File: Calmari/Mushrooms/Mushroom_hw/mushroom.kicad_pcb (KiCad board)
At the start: 2 copper layers, 114 x 16 mm, 56 parts, among them M1 MOTOR_PAD, Q1 MMBT2222, Q2 MMBT2222, Q3 LED_RGB 5050

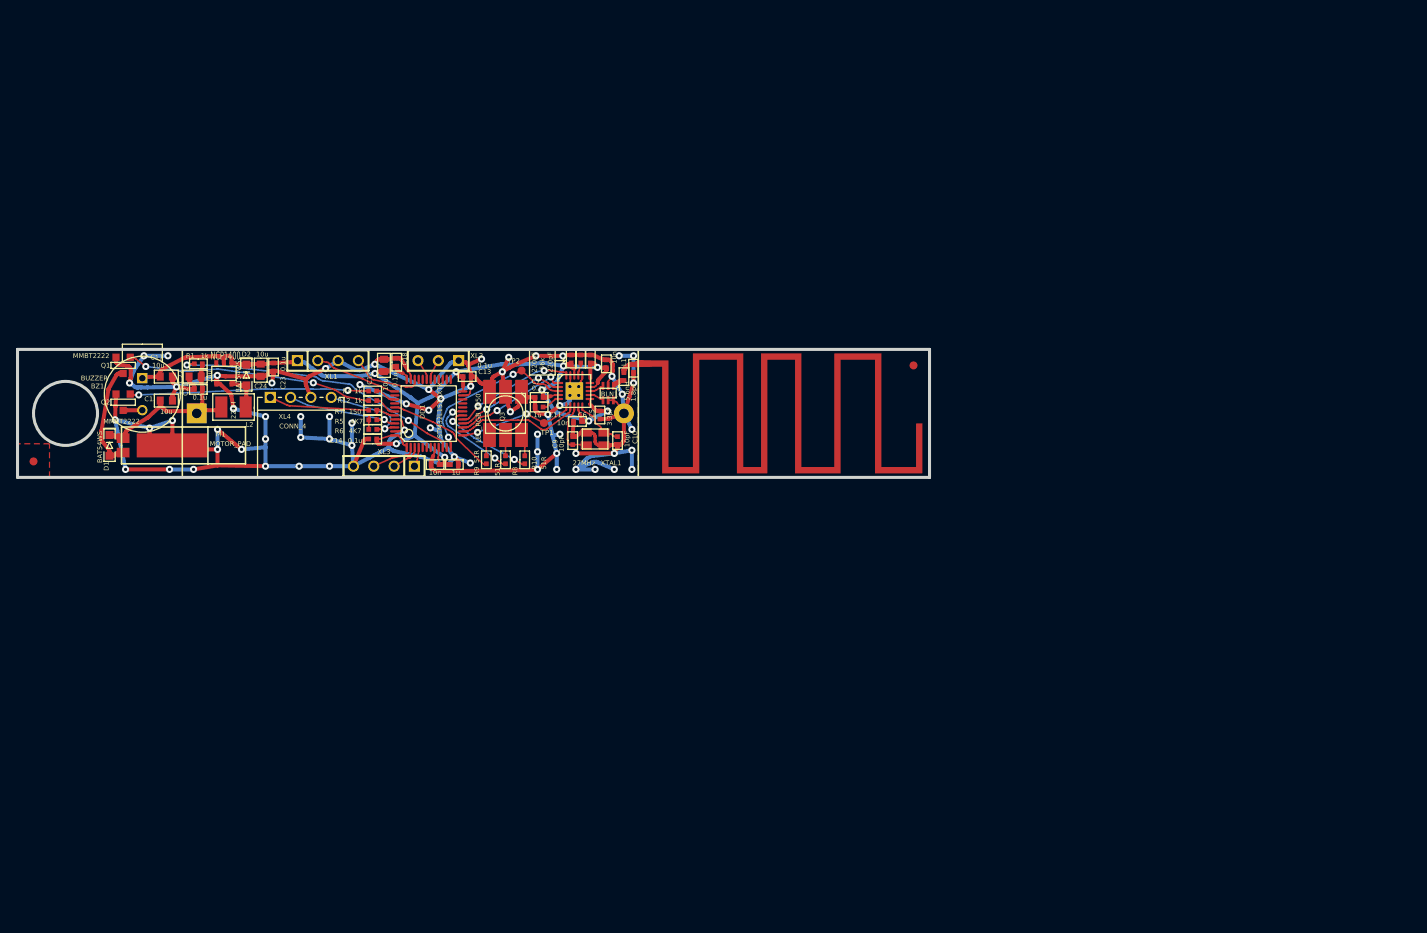
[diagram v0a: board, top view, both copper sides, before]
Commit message: 
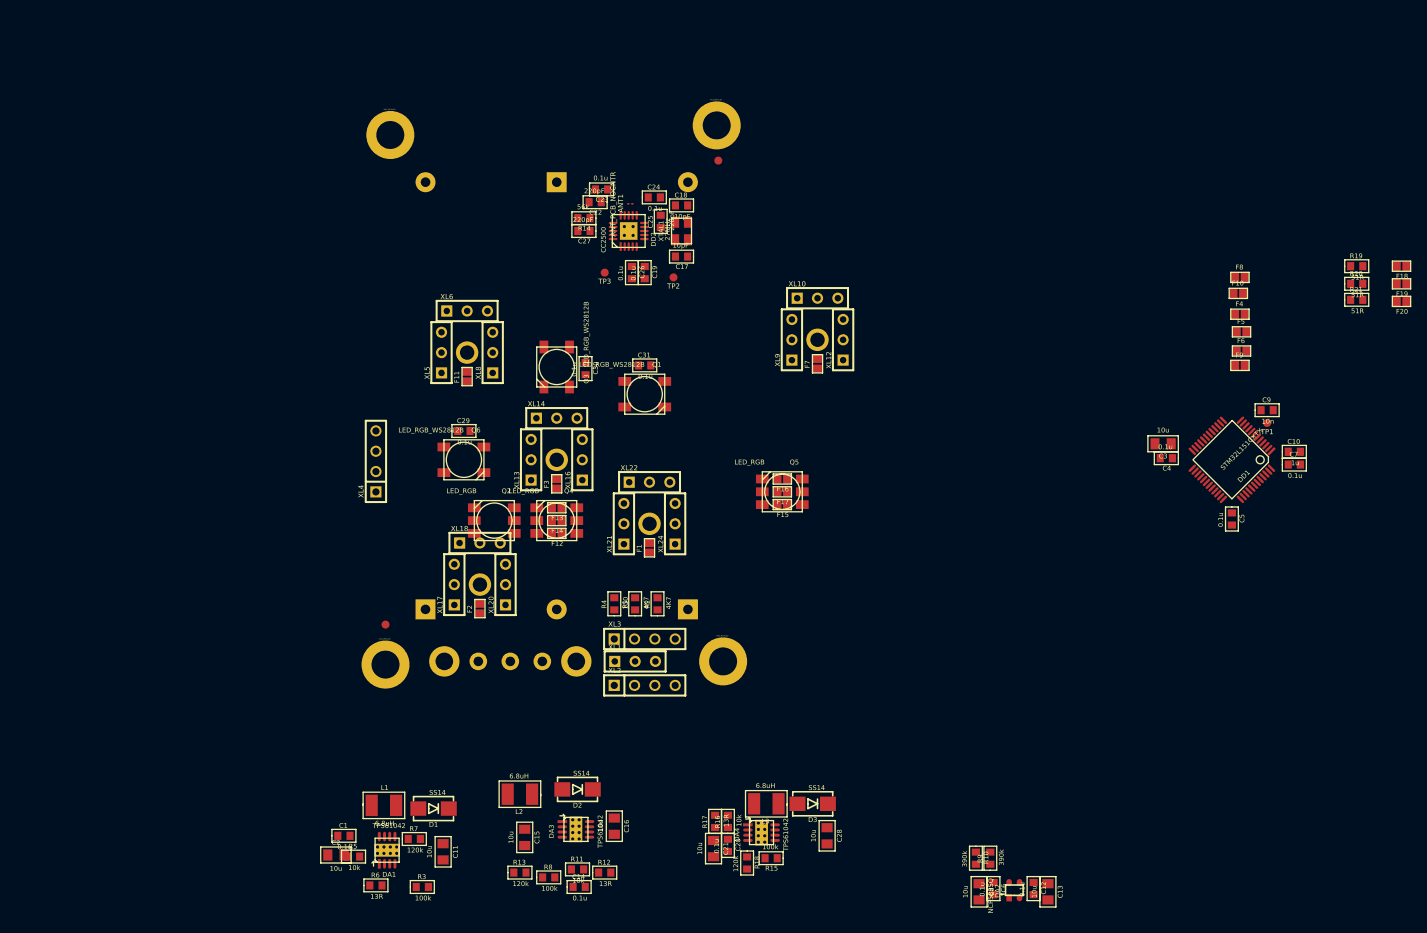
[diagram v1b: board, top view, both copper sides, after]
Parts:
- removed BLN1: 0896BM15A0001, BALUN_JOHANSON868
- removed BZ1: BUZZER, BUZZER_HC0903
- removed M1: MOTOR_PAD, MOTOR_KHN4NX
- added B1: BAT, BAT_AA, B.Cu at (243.8, 178.8)
- added B2: BAT, BAT_AA, B.Cu at (227.4, 178.8)
- added C19: 0.1u, CAP_0603, F.Cu at (238.4, 163.4)
- added C20: 0.1u, CAP_0603, F.Cu at (248.8, 235.0)
- added C25: 220pF, CAP_0603, F.Cu at (240.4, 157.0)
- added C26: 0.1u, CAP_0603, F.Cu at (236.8, 163.4)
- added C27: 220pF, CAP_0603, F.Cu at (230.8, 158.2)
- added C28: 10u, CAP_0805, F.Cu at (261.2, 233.8)
- added C29: 0.1u, CAP_0603, F.Cu at (215.8, 183.2)
- added C30: 0.1u, CAP_0603, F.Cu at (231.0, 175.4)
- added C31: 0.1u, CAP_0603, F.Cu at (238.4, 175.0)
- added D3: SS14, DIODE_SMA_DO214AC, F.Cu at (259.4, 229.8)
- added DA2: NCP583SQ, SC82AB, F.Cu at (284.6, 240.6)
- added DA3: TPS61042, DRB8, F.Cu at (229.8, 233.0)
- added DA4: TPS61042, DRB8, F.Cu at (253.0, 233.4)
- added F1: FUSE0R, SMD0603_FUSE, F.Cu at (239.0, 197.8)
- added F10: FUSE0R, SMD0603_FUSE, F.Cu at (312.6, 166.0)
- added F11: FUSE0R, SMD0603_FUSE, F.Cu at (216.2, 176.4)
- added F12: FUSE0R, SMD0603_FUSE, F.Cu at (227.4, 196.0)
- added F13: FUSE0R, SMD0603_FUSE, F.Cu at (227.4, 192.8)
- added F14: FUSE0R, SMD0603_FUSE, F.Cu at (227.4, 194.4)
- added F15: FUSE0R, SMD0603_FUSE, F.Cu at (255.6, 192.4)
- added F16: FUSE0R, SMD0603_FUSE, F.Cu at (255.6, 189.2)
- added F17: FUSE0R, SMD0603_FUSE, F.Cu at (255.6, 190.8)
- added F18: FUSE0R, SMD0603_FUSE, F.Cu at (333.0, 162.6)
- added F19: FUSE0R, SMD0603_FUSE, F.Cu at (333.0, 164.8)
- added F2: FUSE0R, SMD0603_FUSE, F.Cu at (217.8, 205.4)
- added F20: FUSE0R, SMD0603_FUSE, F.Cu at (333.0, 167.0)
- added F3: FUSE0R, SMD0603_FUSE, F.Cu at (227.4, 189.8)
- added F4: FUSE0R, SMD0603_FUSE, F.Cu at (312.8, 168.6)
- added F5: FUSE0R, SMD0603_FUSE, F.Cu at (313.0, 170.8)
- added F6: FUSE0R, SMD0603_FUSE, F.Cu at (313.0, 173.2)
- added F7: FUSE0R, SMD0603_FUSE, F.Cu at (260.0, 174.8)
- added F8: FUSE0R, SMD0603_FUSE, F.Cu at (312.8, 164.0)
- added F9: FUSE0R, SMD0603_FUSE, F.Cu at (312.8, 175.0)
- added HOLE1: HOLE_METALLED, Hole3_5_out6mm, F.Cu at (206.6, 146.2)
- added HOLE2: HOLE_METALLED, Hole3_5_out6mm, F.Cu at (248.2, 212.0)
- added HOLE3: HOLE_METALLED, Hole3_5_out6mm, F.Cu at (206.0, 212.4)
- added HOLE4: HOLE_METALLED, Hole3_5_out6mm, F.Cu at (247.4, 145.0)
- added L3: 6.8uH, IND_1210, F.Cu at (253.6, 229.8)
- added Q4: LED_RGB, LED_HH5050_RGB, F.Cu at (227.4, 194.4)
- added Q5: LED_RGB, LED_HH5050_RGB, F.Cu at (255.6, 190.8)
- added Q6: LED_RGB_WS2812B, LED_WS2812B, F.Cu at (215.8, 186.8)
- added R11: 10k, RES_0603, F.Cu at (230.0, 238.0)
- added R13: 120k, RES_0603, F.Cu at (222.8, 238.4)
- added R14: 56k, RES_0603, F.Cu at (230.8, 156.6)
- added R15: 100k, RES_0603, F.Cu at (254.2, 236.6)
- added R16: 10k, RES_0603, F.Cu at (248.8, 232.0)
- added R17: 13R, RES_0603, F.Cu at (247.2, 232.0)
- added R18: 120k, RES_0603, F.Cu at (251.2, 237.2)
- added R19: 51R, RES_0603, F.Cu at (327.4, 162.6)
- added R20: 51R, RES_0603, F.Cu at (327.4, 164.8)
- added R21: 51R, RES_0603, F.Cu at (327.4, 166.8)
- added R3: 100k, RES_0603, F.Cu at (210.6, 240.2)
- added SW1: SWITCH_H, SWITCH_SS9, B.Cu at (221.6, 212.0)
- added TP3: TESTPOINT, TESTPOINT_1MM, F.Cu at (233.4, 163.4)
- added XL10: CONN_3, SIL-3, F.Cu at (260.0, 166.6)
- added XL11: CONN_1, SIL1_ROUND_1MM8, F.Cu at (217.8, 202.4)
- added XL12: CONN_3, SIL-3, F.Cu at (263.2, 171.8)
- added XL13: CONN_3, SIL-3, F.Cu at (224.2, 186.8)
- added XL14: CONN_3, SIL-3, F.Cu at (227.4, 181.6)
- added XL15: CONN_1, SIL1_ROUND_1MM8, F.Cu at (227.4, 186.8)
- added XL16: CONN_3, SIL-3, F.Cu at (230.6, 186.8)
- added XL17: CONN_3, SIL-3, F.Cu at (214.6, 202.4)
- added XL18: CONN_3, SIL-3, F.Cu at (217.8, 197.2)
- added XL19: CONN_1, SIL1_ROUND_1MM8, F.Cu at (260.0, 171.8)
- added XL20: CONN_3, SIL-3, F.Cu at (221.0, 202.4)
- added XL21: CONN_3, SIL-3, F.Cu at (235.8, 194.8)
- added XL22: CONN_3, SIL-3, F.Cu at (239.0, 189.6)
- added XL23: CONN_1, SIL1_ROUND_1MM8, F.Cu at (216.2, 173.4)
- added XL24: CONN_3, SIL-3, F.Cu at (242.2, 194.8)
- added XL5: CONN_3, SIL-3, F.Cu at (213.0, 173.4)
- added XL6: CONN_3, SIL-3, F.Cu at (216.2, 168.2)
- added XL7: CONN_1, SIL1_ROUND_1MM8, F.Cu at (239.0, 194.8)
- added XL8: CONN_3, SIL-3, F.Cu at (219.4, 173.4)
- added XL9: CONN_3, SIL-3, F.Cu at (256.8, 171.8)
- ANT1: value ANT_PCB_MONO -> ANT_PCB_NOCNTR; footprint ANT_MEANDER868_16MM -> AntDipole1
- B3: moved to B.Cu
- C1, C12, C24: value 10u -> 0.1u
- C10: value 10pF -> 1u; footprint CAP_0402 -> CAP_0603
- C11, C13, C21: value 0.1u -> 10u; footprint CAP_0402 -> CAP_0805
- C14, C23, C7: footprint CAP_0402 -> CAP_0603
- C15: value 10n -> 10u; footprint CAP_0402 -> CAP_0805
- C16: value 1u -> 10u; footprint CAP_0402 -> CAP_0805
- C17: value 10u -> 10pF
- C18: value 0.1u -> 10pF; footprint CAP_0402 -> CAP_0603
- C2: value 1.8pF -> 10u; footprint CAP_0402 -> CAP_0805
- C22: value 10u -> 220pF
- C3, C8: value 220pF -> 10u; footprint CAP_0402 -> CAP_0805
- C4, C6: value 10n -> 0.1u; footprint CAP_0402 -> CAP_0603
- C5: value 3.3pF -> 0.1u; footprint CAP_0402 -> CAP_0603
- C9: value 10pF -> 10n; footprint CAP_0402 -> CAP_0603
- D1, D2: value BAT54WS -> SS14; footprint DIODE_SOD323 -> DIODE_SMA_DO214AC
- DA1: value NCP1400 -> TPS61042; footprint SOT23-5 -> DRB8
- DD2: value CC1101 -> CC2500
- L1: value 5.6nH -> 6.8uH; footprint IND_0402 -> IND_1210
- L2: value 22uH -> 6.8uH
- Q1: value MMBT2222 -> LED_RGB_WS2812B; footprint SOT23 -> LED_WS2812B
- Q2: value MMBT2222 -> LED_RGB; footprint SOT23 -> LED_HH5050_RGB
- Q3: value LED_RGB 5050 -> LED_RGB_WS2812B; footprint LED_HH5050_RGB -> LED_WS2812B
- R1: value 1k -> 4K7; footprint RES_0402 -> RES_0603
- R10, R9: value 51R -> 390k; footprint RES_0402 -> RES_0603
- R12: value 1k -> 13R; footprint RES_0402 -> RES_0603
- R2: value 56k -> 4K7; footprint RES_0402 -> RES_0603
- R4: value 1k -> 150; footprint RES_0402 -> RES_0603
- R5: value 4K7 -> 10k; footprint RES_0402 -> RES_0603
- R6: value 4K7 -> 13R; footprint RES_0402 -> RES_0603
- R7: value 150 -> 120k; footprint RES_0402 -> RES_0603
- R8: value 51R -> 100k; footprint RES_0402 -> RES_0603
- XL1: value ST_SWD -> CONN_3; footprint SIL-4 -> SIL-3
- XL2: value CONN_3 -> ST_SWD; footprint SIL-3 -> SIL-4
- XL4: footprint CONN_PBS_4R -> SIL-4
- moved C12 104.3 mm to (287.0, 240.4), turned to 270 degrees
- moved DD1 100.6 mm to (311.8, 186.8), turned to 225 degrees
- moved C13 97.0 mm to (288.8, 240.8), turned to 270 degrees
- moved C7 94.8 mm to (319.6, 187.4), turned to 0 degrees
- moved TP1 90.4 mm to (316.2, 182.2)
- moved C9 86.9 mm to (316.2, 180.6), turned to 0 degrees
- moved C21 86.3 mm to (247.0, 235.4), turned to 270 degrees
- moved C10 84.6 mm to (319.6, 185.8), turned to 0 degrees
- moved C8 83.9 mm to (280.2, 240.8), turned to 270 degrees
- moved R9 80.3 mm to (281.6, 236.6)
- moved C5 80.1 mm to (311.8, 194.2)
- moved C6 78.2 mm to (282.0, 240.4), turned to 270 degrees
- moved R10 75.2 mm to (279.8, 236.6), turned to 270 degrees
- moved C3 72.4 mm to (303.2, 184.8), turned to 180 degrees
- moved C2 71.3 mm to (199.8, 236.2), turned to 0 degrees
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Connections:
- net /RED_LED renamed /GREEN_PWM
- ANT1 pad 1: N-0000023 -> /Ant
- B3 pad A: +BATT -> /BAT_IN
- B3 pad C: GND -> N-0000013
- C10 pad 1: N-0000017 -> +3.3V
- C11 pad 1: N-0000015 -> /RED_P
- C14 pad 1: +3.3V -> +BATT
- C15 pad 1: +3.3V -> +BATT
- C16 pad 1: +3.3V -> /GREEN_P
- C17 pad 1: +3.3V -> N-000001
- C18 pad 1: +3.3V -> N-000003
- C2 pad 1: N-0000023 -> +BATT
- C22 pad 1: +BATT -> +3.3V
- C6 pad 1: +3.3V -> +BATT
- C8 pad 1: +3.3V -> +BATT
- C9 pad 1: N-0000018 -> +3.3V
- D1 pad A: /VibroOut -> N-0000018
- D1 pad C: +BATT -> /RED_P
- D2 pad A: /Lout -> N-0000017
- D2 pad C: +3.3V -> /GREEN_P
- DA1 pad 1: +3.3V -> /RED_N
- DA1 pad 2: +3.3V -> N-000004
- DA1 pad 3: (no net) -> +BATT
- DA1 pad 4: GND -> N-000005
- DA1 pad 5: /Lout -> /RED_PWM
- DD1 pad 10: N-0000022 -> N-000006
- DD1 pad 11: (no net) -> /CC_GDO2
- DD1 pad 12: /CC_GDO2 -> /CC_CS
- DD1 pad 14: /CC_CS -> /BRIGHTNESS
- DD1 pad 18: /BLUE_LED -> /RED_PWM
- DD1 pad 2: N-0000038 -> (no net)
- DD1 pad 21: (no net) -> N-0000033
- DD1 pad 22: (no net) -> N-0000034
- DD1 pad 25: (no net) -> N-0000035
- DD1 pad 28: (no net) -> /DIN0
- DD1 pad 3: N-0000037 -> (no net)
- DD1 pad 39: /Buzzer -> (no net)
- DD1 pad 4: N-0000036 -> (no net)
- DD1 pad 41: /GREEN_LED -> /BLUE_PWM
- DD1 pad 42: /Vibro -> (no net)
- DD1 pad 7: (no net) -> N-0000057
- DD2 pad 10: N-0000017 -> N-000003
- DD2 pad 12: /RF1 -> /Ant
- DD2 pad 13: /RF2 -> /Ant
- DD2 pad 17: N-0000019 -> N-0000014
- DD2 pad 5: N-0000015 -> N-0000011
- DD2 pad 8: N-0000018 -> N-000001
- L1 pad 1: N-0000023 -> N-0000018
- L1 pad 2: N-000001 -> +BATT
- L2 pad 1: /Lout -> N-0000017
- Q1 pad 1: N-0000027 -> +BATT
- Q1 pad 2: GND -> N-0000059
- Q1 pad 3: /VibroOut -> GND
- R1 pad 1: N-0000022 -> /P_SCL
- R1 pad 2: +BATT -> /PeriphPwr
- R10 pad 1: /BLUE_LED -> N-000006
- R10 pad 2: N-000002 -> GND
- R12 pad 1: /Vibro -> N-0000015
- R12 pad 2: N-0000027 -> GND
- R2 pad 1: N-0000019 -> /P_SDA
- R2 pad 2: GND -> /PeriphPwr
- R4 pad 1: /Buzzer -> /PeriphPwr1
- R4 pad 2: N-0000012 -> /PeriphPwr
- R5 pad 1: /P_SCL -> N-000004
- R5 pad 2: /PeriphPwr -> N-000005
- R6 pad 1: /P_SDA -> N-000004
- R6 pad 2: /PeriphPwr -> GND
- R7 pad 1: /PeriphPwr1 -> N-000005
- R7 pad 2: /PeriphPwr -> /BRIGHTNESS
- R8 pad 2: N-000003 -> GND
- R9 pad 1: /GREEN_LED -> +BATT
- R9 pad 2: N-000004 -> N-000006
- TP1 pad 1: /CC_GDO0 -> N-0000057
- TP2 pad 1: /CC_GDO2 -> /CC_GDO0
- XL1 pad 1: +3.3V -> GND
- XL1 pad 2: /SWCLK -> /UART_TX
- XL1 pad 3: GND -> /UART_RX
- XL2 pad 1: GND -> +3.3V
- XL2 pad 2: /UART_TX -> /SWCLK
- XL2 pad 3: /UART_RX -> GND
- XL3 pad 1: N-0000036 -> /PeriphPwr1
- XL3 pad 2: N-0000037 -> /P_SCL
- XL3 pad 3: N-0000038 -> GND
- XL3 pad 4: GND -> /P_SDA
- XL4 pad 1: /PeriphPwr1 -> N-0000033
- XL4 pad 2: /P_SCL -> N-0000034
- XL4 pad 3: GND -> N-0000035
- XL4 pad 4: /P_SDA -> GND
- XTAL1 pad 1: N-0000018 -> N-000001
- XTAL1 pad 2: N-0000017 -> N-000003
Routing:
- net GND: track 379.0 -> 0.00 mm, vias 66 -> 0
- net +3.3V: track 133.1 -> 0.00 mm, vias 9 -> 0
- net N-0000022: track 35.9 -> 0.00 mm, vias 2 -> 0
- net N-0000027: track 30.8 -> 0.00 mm, vias 2 -> 0
- net N-0000012: track 29.9 -> 0.00 mm, vias 2 -> 0
- net +BATT: track 24.1 -> 0.00 mm
- net /CC_GDO2: track 21.2 -> 0.00 mm, vias 2 -> 0
- net /CC_CS: track 15.6 -> 0.00 mm
- net /CC_MOSI: track 15.3 -> 0.00 mm, vias 2 -> 0
- net /CC_GDO0: track 14.6 -> 0.00 mm, vias 2 -> 0
- net /P_SCL: track 14.5 -> 0.00 mm, vias 1 -> 0
- net /CC_SCK: track 14.3 -> 0.00 mm, vias 2 -> 0
- net /CC_MISO: track 14.0 -> 0.00 mm, vias 2 -> 0
- net /GREEN_LED: track 13.8 -> 0.00 mm
- net /VibroOut: track 13.5 -> 0.00 mm
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- removed copper zone on B.Cu, net GND
- removed copper zone on F.Cu, net GND
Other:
- board outline removed
- net class Default: clearance 0.2 -> 0.254; trace_width 0.2 -> 0.254; via_dia 0.9 -> 0.889; via_drill 0.4 -> 0.635
- net class Wide removed
- rule pad_to_mask_clearance: 0.1 -> 0.2
- rule trace_clearance: 0.2 -> 0.254
- rule trace_min: 0.2 -> 0.254
- rule via_min_drill: 0.3 -> 0.508
- rule via_min_size: 0.9 -> 0.889

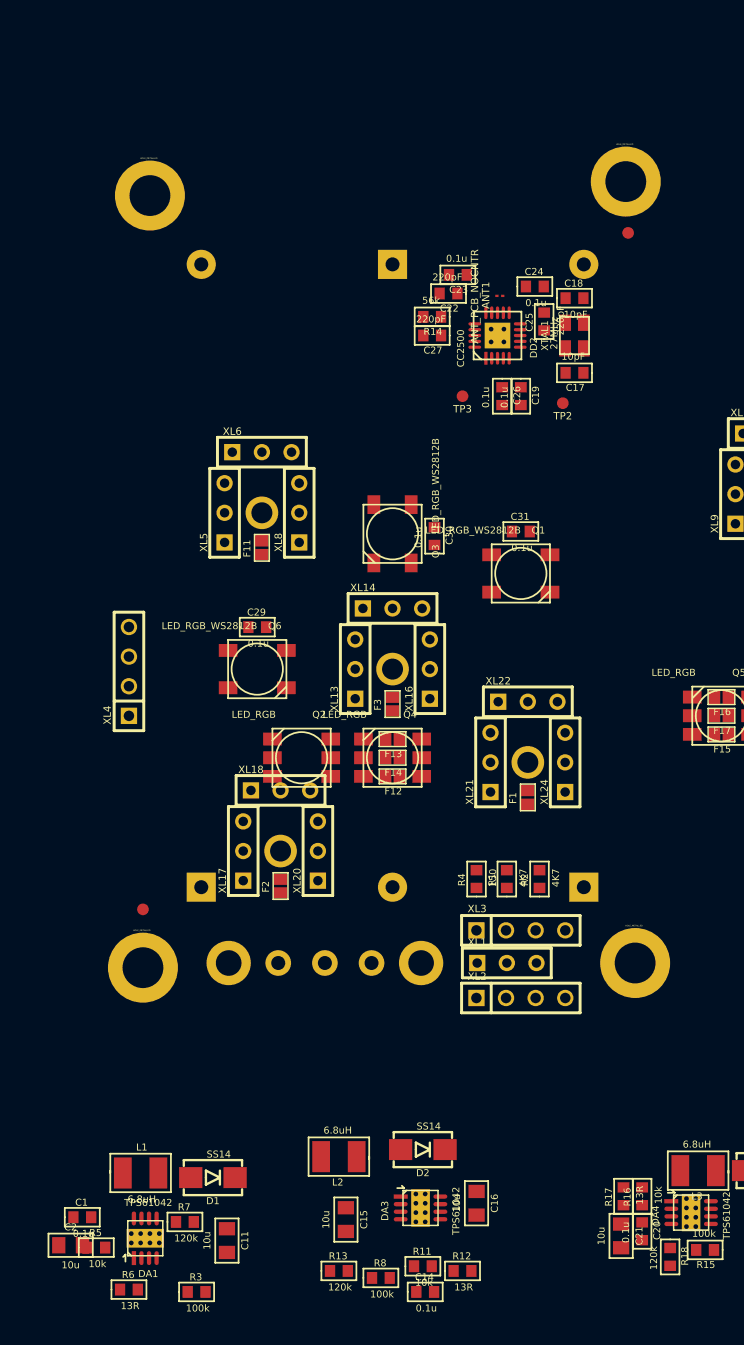
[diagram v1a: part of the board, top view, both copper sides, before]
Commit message: Proceeding with mushroom PCB
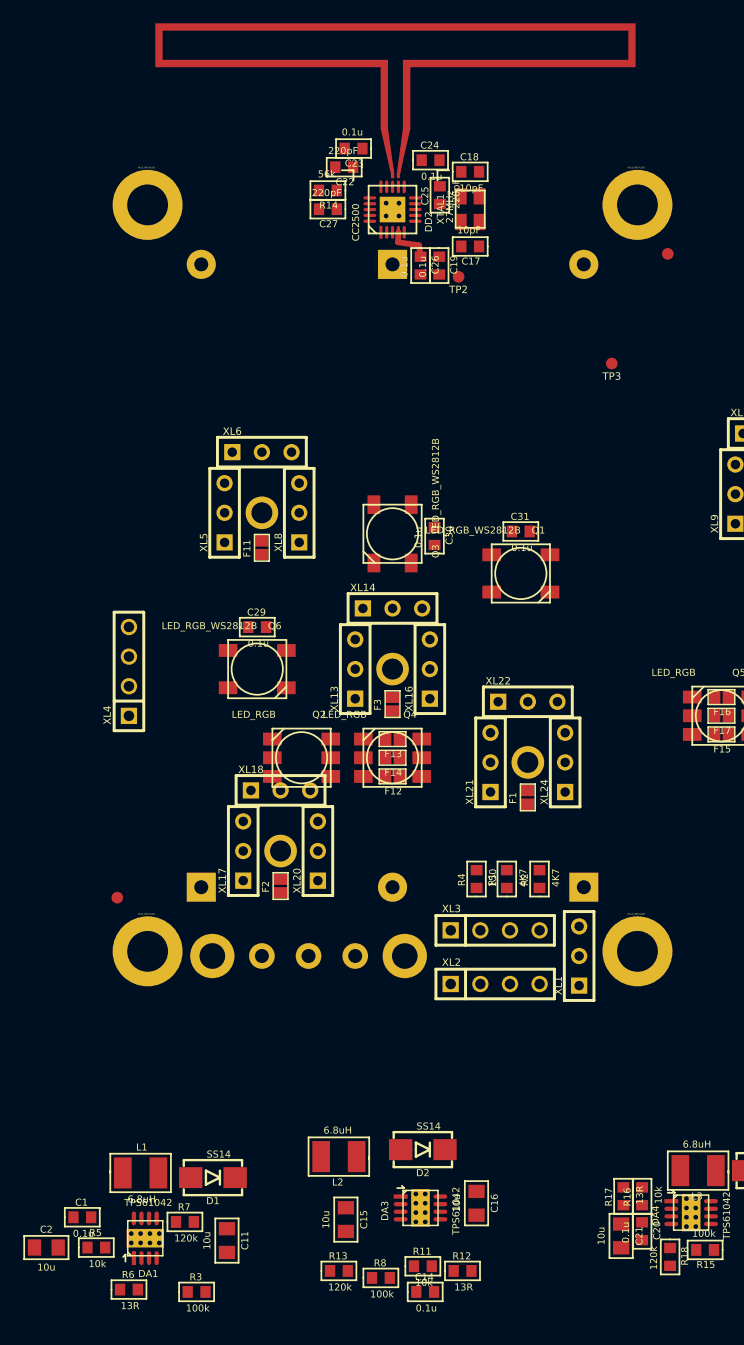
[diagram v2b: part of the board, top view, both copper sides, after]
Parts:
- ANT1: footprint AntDipole1 -> ANT_FOLDED_DIPOLE2
- moved ANT1 16.9 mm to (227.7, 140.5)
- moved DD2 14.1 mm to (227.4, 147.4)
- moved C25 14.0 mm to (231.5, 146.2)
- moved C17 14.0 mm to (234.1, 150.6)
- moved C18 14.0 mm to (234.1, 144.2)
- moved C23 14.0 mm to (224.1, 142.2)
- moved C24 14.0 mm to (230.7, 143.2)
- moved TP2 14.0 mm to (233.1, 153.2)
- moved C27 14.0 mm to (221.9, 147.4)
- moved R14 14.0 mm to (221.9, 145.8)
- moved C22 14.0 mm to (223.3, 143.8)
- moved XTAL1 14.0 mm to (234.1, 147.4)
- moved C19 13.2 mm to (231.4, 152.2)
- moved C26 13.2 mm to (229.8, 152.2)
- moved TP3 13.1 mm to (246.2, 160.6)
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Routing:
- net +3.3V: track 0.00 -> 3.65 mm
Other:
- net class Default: clearance 0.254 -> 0.2; trace_width 0.254 -> 0.2; via_dia 0.889 -> 0.9; via_drill 0.635 -> 0.4
- net class Wide added: clearance 0.2, trace_width 0.5, via_dia 0.9, via_drill 0.4
- rule trace_clearance: 0.254 -> 0.2
- rule trace_min: 0.254 -> 0.2
- rule via_min_drill: 0.508 -> 0.4

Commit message: PCB completed
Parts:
- moved F19 118.7 mm to (215.0, 177.6), turned to 90 degrees
- moved F18 118.6 mm to (215.0, 175.0), turned to 270 degrees
- moved F20 118.1 mm to (215.0, 172.4), turned to 270 degrees
- moved F4 99.8 mm to (216.6, 195.2)
- moved F5 98.9 mm to (216.6, 192.8)
- moved F6 97.9 mm to (216.6, 190.2)
- moved R19 86.7 mm to (241.6, 175.4), turned to 180 degrees
- moved R20 86.7 mm to (241.6, 177.2), turned to 180 degrees
- moved R21 86.1 mm to (241.6, 173.6), turned to 180 degrees
- moved F8 80.9 mm to (238.2, 195.2)
- moved F10 78.2 mm to (238.2, 190.2)
- moved F9 76.7 mm to (238.2, 192.8)
- moved C5 74.2 mm to (237.8, 199.0), turned to 180 degrees
- moved C7 73.2 mm to (248.2, 203.6), turned to 270 degrees
- moved R6 71.1 mm to (208.4, 169.0)
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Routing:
- net GND: track 0.00 -> 812.5 mm, vias 0 -> 151
- net +3.3V: track 3.65 -> 177.8 mm, vias 0 -> 10
- net +BATT: track 0.00 -> 159.2 mm, vias 0 -> 2
- net /BLUE_P: track 0.00 -> 78.3 mm, vias 0 -> 1
- net /BRIGHTNESS: track 0.00 -> 73.8 mm, vias 0 -> 4
- net /BLUE_PWM: track 0.00 -> 68.9 mm, vias 0 -> 2
- net /GREEN_P: track 0.00 -> 62.2 mm, vias 0 -> 1
- net /GREEN_PWM: track 0.00 -> 61.7 mm, vias 0 -> 2
- net /RED_N: track 0.00 -> 60.8 mm, vias 0 -> 3
- net /RED_PWM: track 0.00 -> 58.2 mm, vias 0 -> 2
- net /BLUE_N: track 0.00 -> 58.1 mm, vias 0 -> 4
- net /CC_GDO2: track 0.00 -> 58.0 mm
- net /DIN0: track 0.00 -> 57.0 mm, vias 0 -> 1
- net /CC_MOSI: track 0.00 -> 55.4 mm
- net /CC_MISO: track 0.00 -> 55.0 mm
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- added copper zone on B.Cu, net GND
- added copper zone on F.Cu, net GND
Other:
- board outline added: 49.2 x 83.8 mm
- rule pad_to_mask_clearance: 0.2 -> 0.1
